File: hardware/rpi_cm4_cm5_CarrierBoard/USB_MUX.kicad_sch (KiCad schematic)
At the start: 5 parts, among them U22 FSUSB42UMX

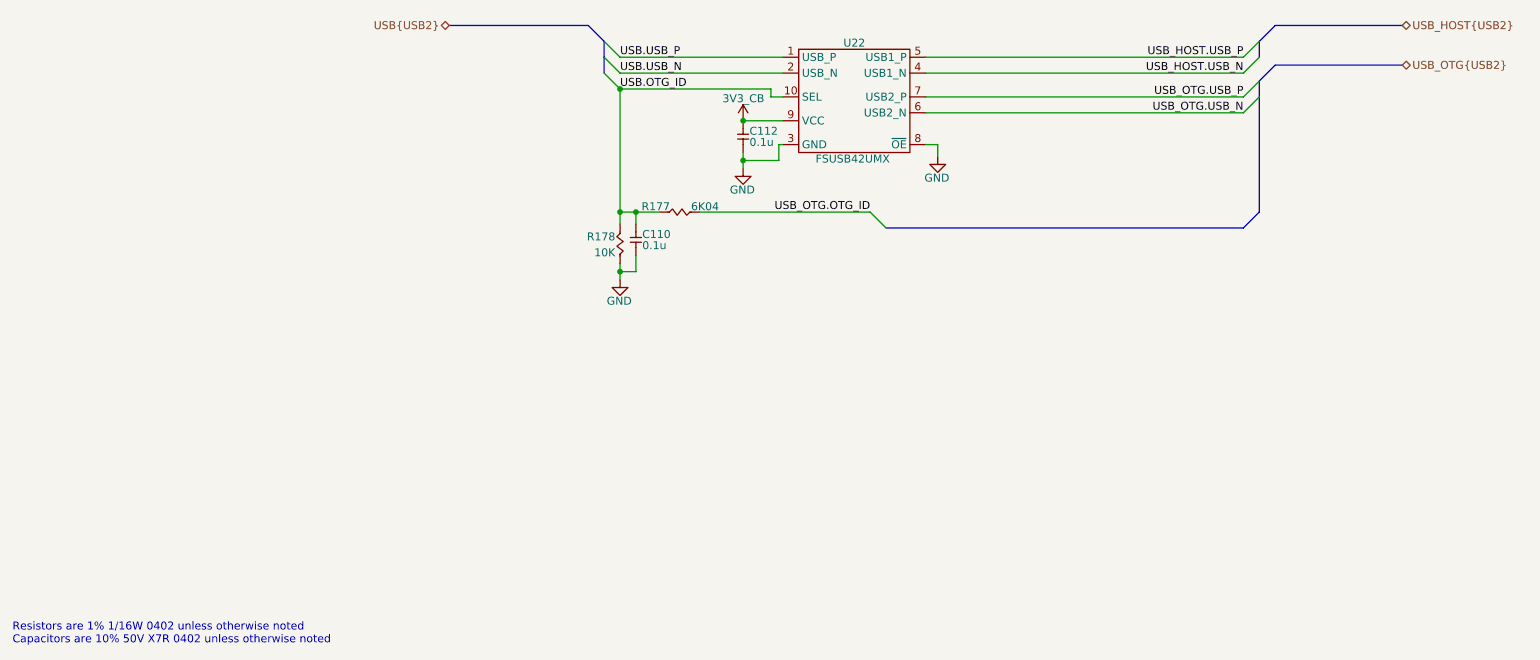
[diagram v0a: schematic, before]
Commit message: Add power-up and power kill sequences Modify schematics to add net classes for DiffPairs
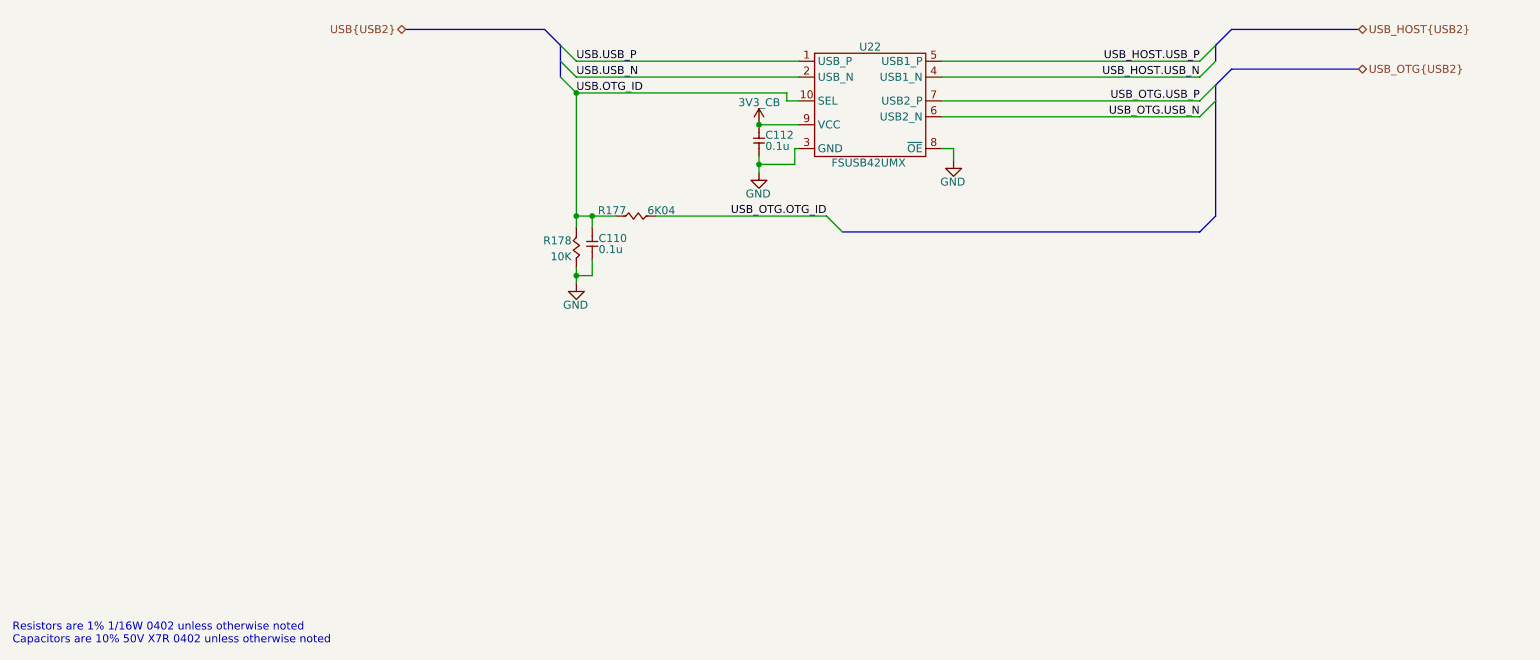
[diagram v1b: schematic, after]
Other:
- moved on the sheet: C110, C112, R177, R178, U22

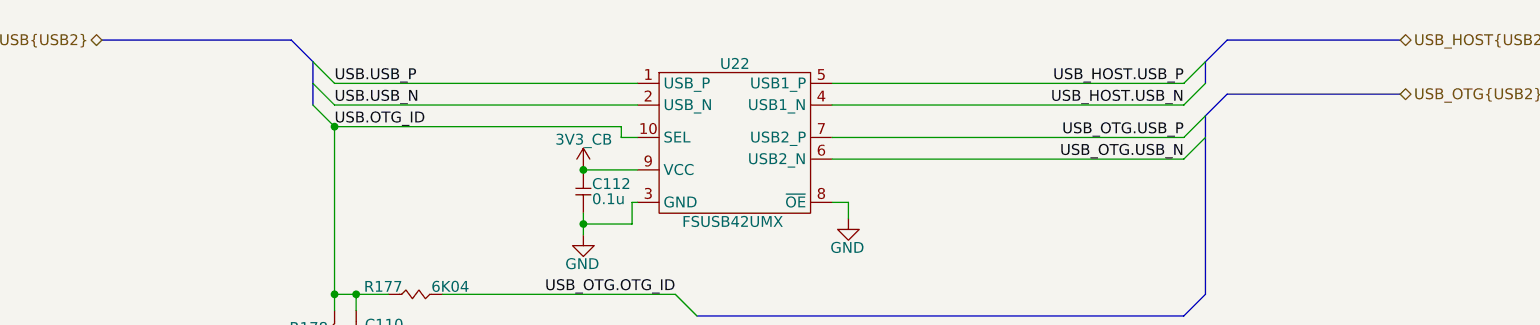
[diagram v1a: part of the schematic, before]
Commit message: Significant update to schematics Add codec, Mikrobus, PIC32A Add power table, design notes for pinmux Add datasheets
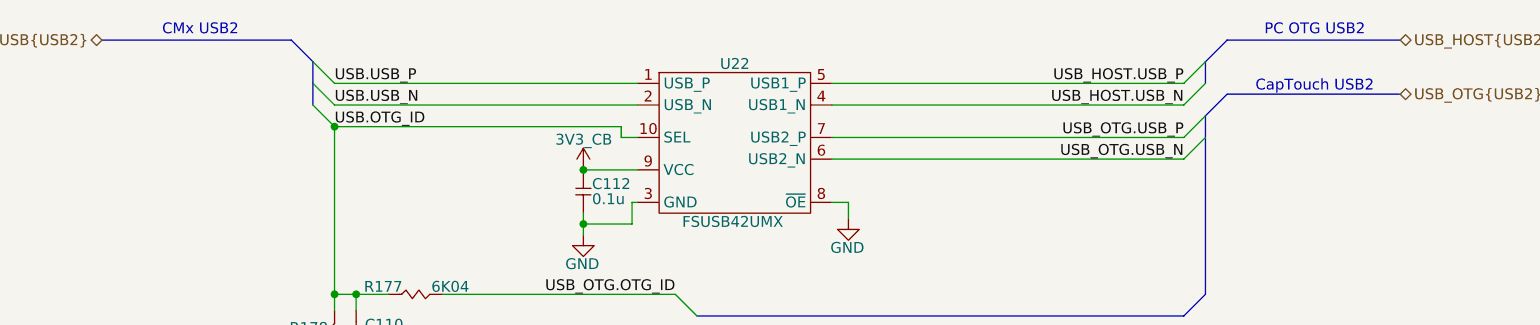
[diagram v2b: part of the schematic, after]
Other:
- note added: "CMx USB2"
- note added: "CapTouch USB2"
- note added: "PC OTG USB2"
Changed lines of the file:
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@@
 		(comment 8 "WIP")
+	)
+	(text "CapTouch USB2"
+		(exclude_from_sim no)
+		(at 217.932 79.756 0)
+		(effects
+			(font
+				(size 1.27 1.27)
+				(color 255 153 0 1)
+			)
+		)
 	)
 	(text "Resistors are 1% 1/16W 0402 unless otherwise noted\nCapacitors are 10% 50V X7R 0402 unless otherwise noted"
@@
 		)
 	)
+	(text "CMx USB2"
+		(exclude_from_sim no)
+		(at 87.122 73.152 0)
+		(effects
+			(font
+				(size 1.27 1.27)
+				(color 255 153 0 1)
+			)
+		)
+	)
+	(text "PC OTG USB2"
+		(exclude_from_sim no)
+		(at 217.932 73.152 0)
+		(effects
+			(font
+				(size 1.27 1.27)
+				(color 255 153 0 1)
+			)
+		)
+	)
